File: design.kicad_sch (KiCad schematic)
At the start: 78 parts, among them J1 2601-3108, J10 Conn_01x04, J11 Conn_01x04, J12 Conn_01x03, J13 Conn_01x03, J14 Conn_01x04, J2 2601-3108, J3 2601-3108, J4 TYPE-C-31-M-12, J5 SKEDD-UPDI-4, J6 Conn_01x04, J7 Conn_01x04, J8 Conn_01x04, J9 Conn_01x04, U1 ATtiny1616-S, U2 AP2112K-3.3, U3 CP2105

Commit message: cleanup
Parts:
- added JP4: LED2x2, Jumper:SolderJumper-2_P1.3mm_Open_Pad1.0x1.5mm, symbol Jumper:SolderJumper_2_Open
- JP1: value SolderJumper_2_Bridged -> PC0
- JP2: value SolderJumper_2_Bridged -> PB1
- JP3: value SolderJumper_2_Bridged -> PB2
- TP1, TP2: value TestPoint -> GND
- TP3: value TestPoint -> 3V3
- TP4: value TestPoint -> VDD
- TP5: value TestPoint -> VBUS
- TP6: value RCWCTE -> VDD
- TP7: value RCWCTE -> GND
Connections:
- net LED-out-Bridge: now reaches LED6.1 (DO), LED7.3 (DI)
- net LED-out-Bridge: now also JP4.2 (B)
- net LED-in-Bridge: now reaches LED2.1 (DO), LED3.3 (DI)
- net LED-in-Bridge: now also JP4.1 (A)
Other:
- moved on the sheet: JP1, JP2, JP3

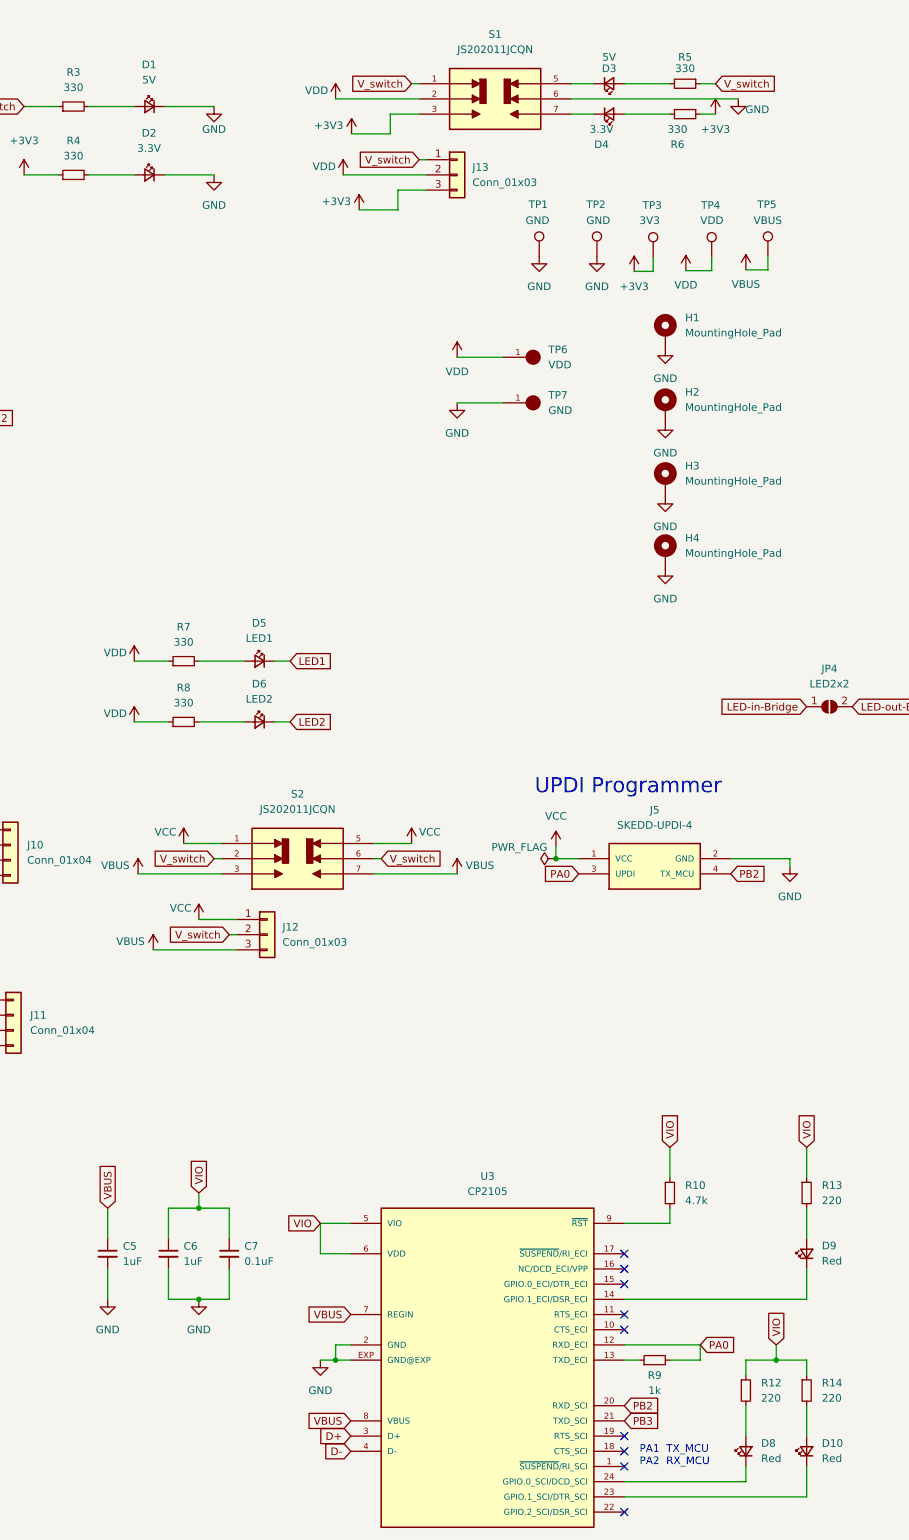
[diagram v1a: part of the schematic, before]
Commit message: add LED color and Parameters
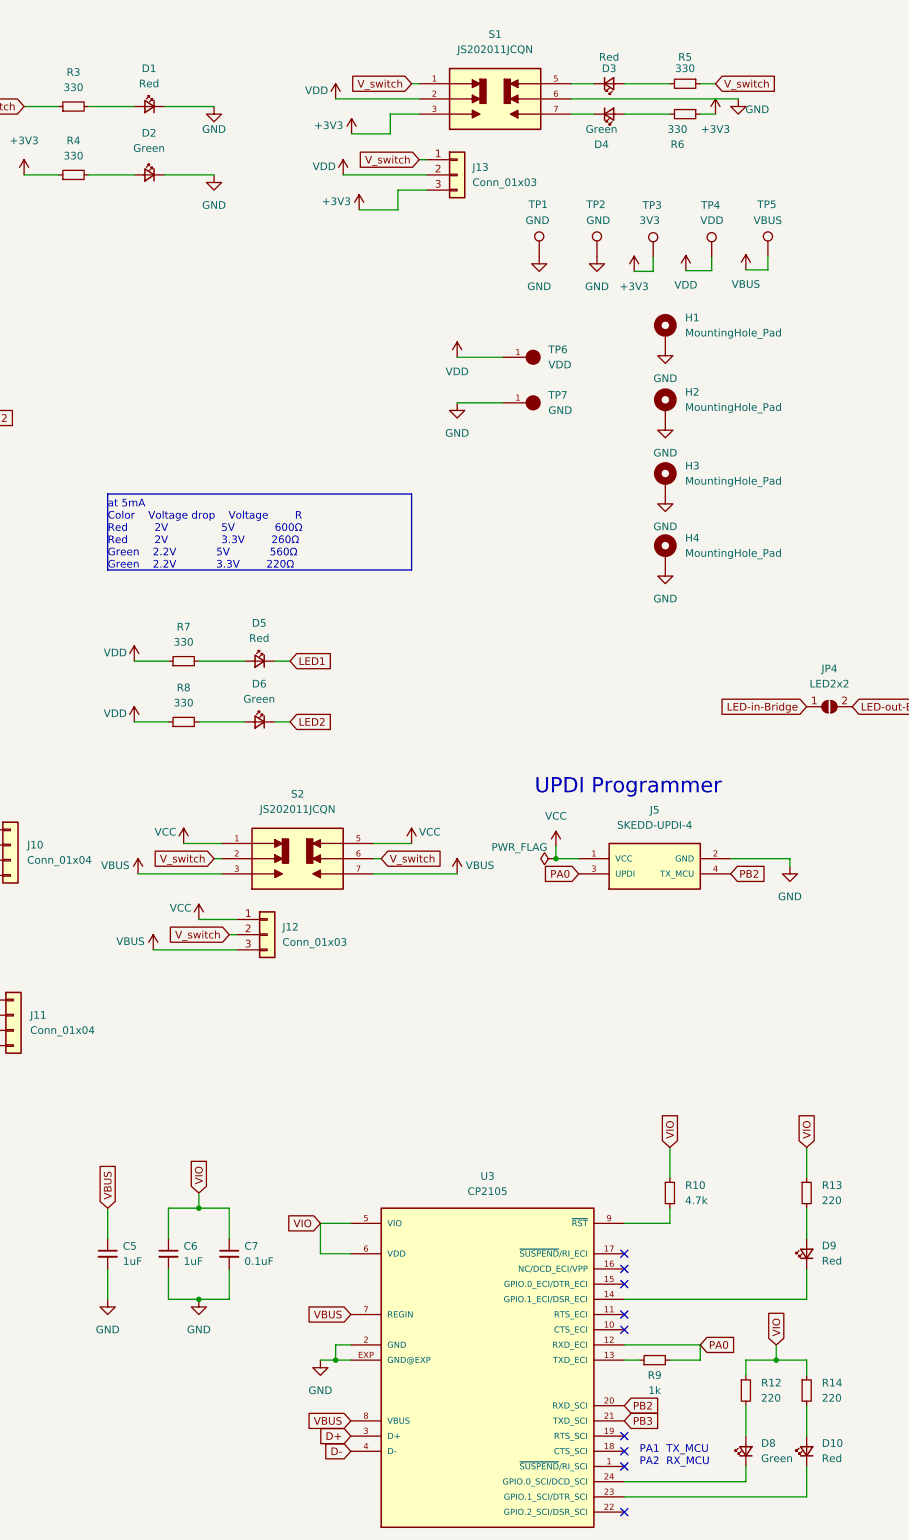
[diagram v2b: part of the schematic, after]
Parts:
- D1, D3: value 5V -> Red
- D2, D4: value 3.3V -> Green
- D5: value LED1 -> Red
- D6: value LED2 -> Green
- D8: value Red -> Green
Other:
- note added: "at 5mA Color Voltage drop Voltage R Red 2V 5V 600Ω Red 2V 3.3V 260Ω Green 2.2V 5V 560Ω Green 2.2V 3.3V 220Ω"
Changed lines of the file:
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@@
     (stroke (width 0) (type default) (color 0 0 0 0))
   )
+  (polyline (pts (xy 213.36 93.98) (xy 213.36 106.68))
+    (stroke (width 0) (type default) (color 0 0 0 0))
+  )
   (wire (pts (xy 182.88 167.64) (xy 184.15 167.64))
     (stroke (width 0) (type default) (color 0 0 0 0))
@@
     (stroke (width 0) (type default) (color 0 0 0 0))
   )
+  (polyline (pts (xy 213.36 106.68) (xy 162.56 106.68))
+    (stroke (width 0) (type default) (color 0 0 0 0))
+  )
   (wire (pts (xy 68.58 27.94) (xy 72.39 27.94))
     (stroke (width 0) (type default) (color 0 0 0 0))
@@
     (stroke (width 0) (type default) (color 0 0 0 0))
   )
+  (polyline (pts (xy 162.56 93.98) (xy 162.56 106.68))
+    (stroke (width 0) (type default) (color 0 0 0 0))
+  )
   (wire (pts (xy 64.77 180.34) (xy 71.12 180.34))
     (stroke (width 0) (type default) (color 0 0 0 0))
@@
     (stroke (width 0) (type default) (color 0 0 0 0))
   )
+  (polyline (pts (xy 162.56 93.98) (xy 213.36 93.98))
+    (stroke (width 0) (type default) (color 0 0 0 0))
+  )
   (wire (pts (xy 358.14 185.42) (xy 358.14 180.34))
     (stroke (width 0) (type default) (color 0 0 0 0))
@@
     (effects (font (size 1.27 1.27)) (justify left bottom))
   )
+  (text "at 5mA\nColor	Voltage drop	Voltage    	R\nRed		2V				5V			600Ω\nRed		2V				3.3V		260Ω\nGreen	2.2V			5V			560Ω\nGreen	2.2V			3.3V		220Ω"
+    (at 162.56 106.68 0)
+    (effects (font (size 1.27 1.27)) (justify left bottom))
+  )
   (text "Output Current: 600mA (Min.)" (at 101.6 58.42 0)
     (effects (font (size 1.27 1.27)) (justify left bottom))
@@
     (in_bom yes) (on_board yes) (fields_autoplaced)
     (property "Reference" "D6" (id 0) (at 187.8965 125.73 0))
-    (property "Value" "LED2" (id 1) (at 187.8965 128.27 0))
+    (property "Value" "Green" (id 1) (at 187.8965 128.27 0))
     (property "Footprint" "LED_SMD:LED_0805_2012Metric" (id 2) (at 187.96 132.08 90)
       (effects (font (size 1.27 1.27)) hide)
@@
     (in_bom yes) (on_board yes) (fields_autoplaced)
     (property "Reference" "D5" (id 0) (at 187.8965 115.57 0))
-    (property "Value" "LED1" (id 1) (at 187.8965 118.11 0))
+    (property "Value" "Red" (id 1) (at 187.8965 118.11 0))
     (property "Footprint" "LED_SMD:LED_0805_2012Metric" (id 2) (at 187.96 121.92 90)
       (effects (font (size 1.27 1.27)) hide)
@@
   (symbol (lib_id "Device:LED_Small") (at 169.545 29.21 0) (mirror y) (unit 1)
     (in_bom yes) (on_board yes) (fields_autoplaced)
-    (property "Reference" "D1" (id 0) (at 169.4815 22.225 0))
-    (property "Value" "5V" (id 1) (at 169.4815 24.765 0))
+    (property "Reference" "D1" (id 0) (at 169.4815 22.86 0))
+    (property "Value" "Red" (id 1) (at 169.4815 25.4 0))
     (property "Footprint" "LED_SMD:LED_0805_2012Metric" (id 2) (at 169.545 29.21 90)
       (effects (font (size 1.27 1.27)) hide)
@@
     (in_bom yes) (on_board yes)
     (property "Reference" "D2" (id 0) (at 169.4815 33.655 0))
-    (property "Value" "3.3V" (id 1) (at 169.4815 36.195 0))
+    (property "Value" "Green" (id 1) (at 169.4815 36.195 0))
     (property "Footprint" "LED_SMD:LED_0805_2012Metric" (id 2) (at 169.545 40.64 90)
       (effects (font (size 1.27 1.27)) hide)
@@
     (in_bom yes) (on_board yes)
     (property "Reference" "D4" (id 0) (at 245.11 35.56 0))
-    (property "Value" "3.3V" (id 1) (at 245.11 33.02 0))
+    (property "Value" "Green" (id 1) (at 245.11 33.02 0))
     (property "Footprint" "LED_SMD:LED_0805_2012Metric" (id 2) (at 246.38 30.48 90)
       (effects (font (size 1.27 1.27)) hide)
@@
     (in_bom yes) (on_board yes)
     (property "Reference" "D3" (id 0) (at 246.38 22.86 0))
-    (property "Value" "5V" (id 1) (at 246.38 20.955 0))
+    (property "Value" "Red" (id 1) (at 246.38 20.955 0))
     (property "Footprint" "LED_SMD:LED_0805_2012Metric" (id 2) (at 246.38 25.4 90)
       (effects (font (size 1.27 1.27)) hide)
@@
       (effects (font (size 1.27 1.27)) (justify right))
     )
-    (property "Value" "Red" (id 1) (at 271.78 255.2064 90)
+    (property "Value" "Green" (id 1) (at 271.78 255.2064 90)
       (effects (font (size 1.27 1.27)) (justify right))
     )
@@
     )
     (path "/5ec38a02-a145-4acb-a554-76dbb10c2abb"
-      (reference "D1") (unit 1) (value "5V") (footprint "LED_SMD:LED_0805_2012Metric")
+      (reference "D1") (unit 1) (value "Red") (footprint "LED_SMD:LED_0805_2012Metric")
     )
     (path "/ab09947a-b17e-4c8a-af0d-4d89f0118870"
-      (reference "D2") (unit 1) (value "3.3V") (footprint "LED_SMD:LED_0805_2012Metric")
+      (reference "D2") (unit 1) (value "Green") (footprint "LED_SMD:LED_0805_2012Metric")
     )
     (path "/c4e31e83-e009-4ac7-b84c-cd948c6ad197"
-      (reference "D3") (unit 1) (value "5V") (footprint "LED_SMD:LED_0805_2012Metric")
+      (reference "D3") (unit 1) (value "Red") (footprint "LED_SMD:LED_0805_2012Metric")
     )
     (path "/c2daad8d-2742-47e3-bd21-622154e104d5"
-      (reference "D4") (unit 1) (value "3.3V") (footprint "LED_SMD:LED_0805_2012Metric")
+      (reference "D4") (unit 1) (value "Green") (footprint "LED_SMD:LED_0805_2012Metric")
     )
     (path "/302ed775-0a92-4094-a83f-5413aa9513d3"
-      (reference "D5") (unit 1) (value "LED1") (footprint "LED_SMD:LED_0805_2012Metric")
+      (reference "D5") (unit 1) (value "Red") (footprint "LED_SMD:LED_0805_2012Metric")
     )
     (path "/29fe1901-f65d-4535-96e4-7f5c316c5cf9"
-      (reference "D6") (unit 1) (value "LED2") (footprint "LED_SMD:LED_0805_2012Metric")
+      (reference "D6") (unit 1) (value "Green") (footprint "LED_SMD:LED_0805_2012Metric")
     )
     (path "/db5ca8c2-4986-41e1-aec1-ef6e7f873716"
-      (reference "D8") (unit 1) (value "Red") (footprint "LED_SMD:LED_0805_2012Metric")
+      (reference "D8") (unit 1) (value "Green") (footprint "LED_SMD:LED_0805_2012Metric")
     )
     (path "/1bc50256-ad94-4b85-ac96-eae729d6ff85"

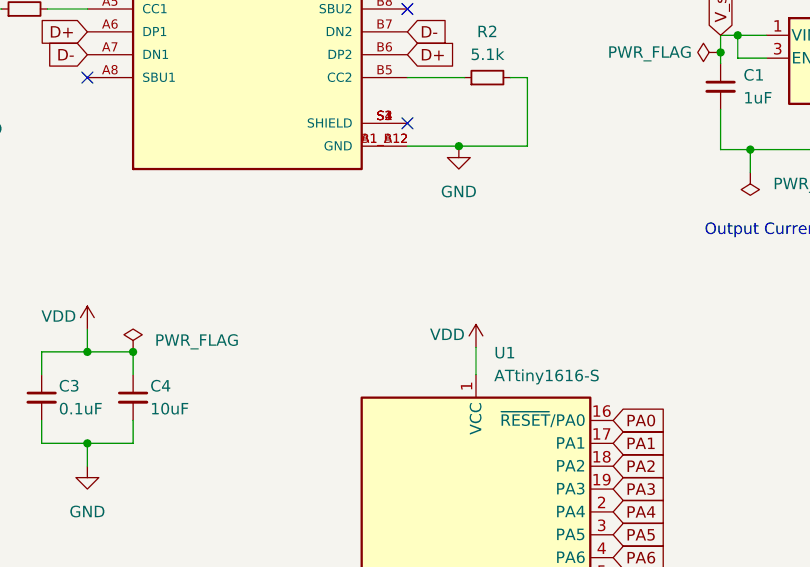
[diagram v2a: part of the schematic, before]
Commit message: Add TVS Diode to USB
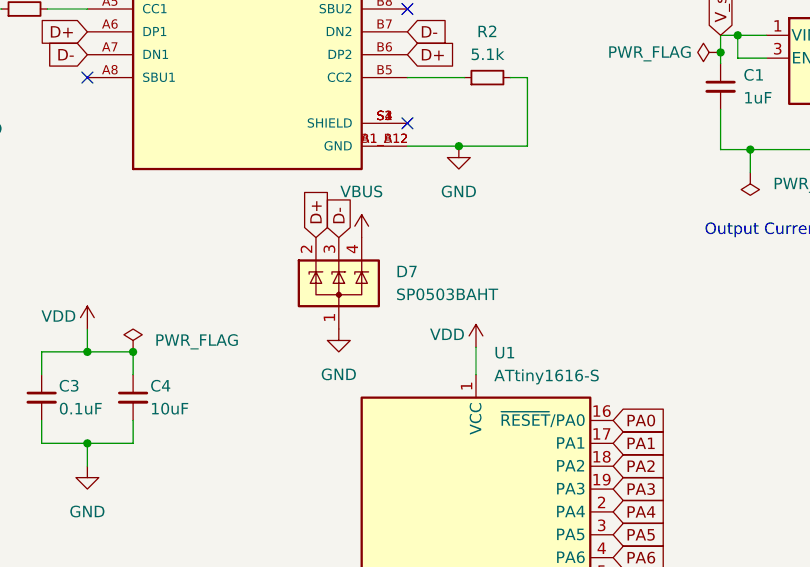
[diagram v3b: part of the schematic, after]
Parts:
- added D7: SP0503BAHT, Package_TO_SOT_SMD:SOT-143, symbol Power_Protection:SP0503BAHT
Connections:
- net D+: now also D7.2 (K)
- net D-: now also D7.3 (K)
- net GND: now also D7.1 (A)
- net VBUS: now also D7.4 (K)
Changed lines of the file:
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@@
     )
   )
+  (global_label "D-" (shape input) (at 60.96 58.42 90) (fields_autoplaced)
+    (effects (font (size 1.27 1.27)) (justify left))
+    (property "Referenzen zwischen Schaltplänen" "${INTERSHEET_REFS}" (id 0) (at 60.8806 53.2534 90)
+      (effects (font (size 1.27 1.27)) (justify left) hide)
+    )
+  )
   (global_label "PA7" (shape input) (at 91.44 96.52 0) (fields_autoplaced)
     (effects (font (size 1.27 1.27)) (justify left))
@@
     )
   )
+  (global_label "D+" (shape input) (at 58.42 58.42 90) (fields_autoplaced)
+    (effects (font (size 1.27 1.27)) (justify left))
+    (property "Referenzen zwischen Schaltplänen" "${INTERSHEET_REFS}" (id 0) (at 58.4994 53.2534 90)
+      (effects (font (size 1.27 1.27)) (justify left) hide)
+    )
+  )
   (global_label "VIO" (shape input) (at 198.12 215.9 180) (fields_autoplaced)
     (effects (font (size 1.27 1.27)) (justify right))
@@
     (pin "4")
   )
+  (symbol (lib_id "power:GND") (at 60.96 68.58 0) (unit 1)
+    (in_bom yes) (on_board yes) (fields_autoplaced)
+    (property "Reference" "#PWR0188" (id 0) (at 60.96 74.93 0)
+      (effects (font (size 1.27 1.27)) hide)
+    )
+    (property "Value" "GND" (id 1) (at 60.96 73.66 0))
+    (property "Footprint" "" (id 2) (at 60.96 68.58 0)
+      (effects (font (size 1.27 1.27)) hide)
+    )
+    (property "Datasheet" "" (id 3) (at 60.96 68.58 0)
+      (effects (font (size 1.27 1.27)) hide)
+    )
+    (pin "1")
+  )
   (symbol (lib_id "power:VCC") (at 175.26 152.4 0) (unit 1)
     (in_bom yes) (on_board yes)
@@
     (pin "1")
   )
+  (symbol (lib_id "Power_Protection:SP0503BAHT") (at 60.96 63.5 0) (unit 1)
+    (in_bom yes) (on_board yes) (fields_autoplaced)
+    (property "Reference" "D7" (id 0) (at 67.31 62.2299 0)
+      (effects (font (size 1.27 1.27)) (justify left))
+    )
+    (property "Value" "SP0503BAHT" (id 1) (at 67.31 64.7699 0)
+      (effects (font (size 1.27 1.27)) (justify left))
+    )
+    (property "Footprint" "Package_TO_SOT_SMD:SOT-143" (id 2) (at 66.675 64.77 0)
+      (effects (font (size 1.27 1.27)) (justify left) hide)
+    )
+    (property "Datasheet" "http://www.littelfuse.com/~/media/files/littelfuse/technical%20resources/documents/data%20sheets/sp05xxba.pdf" (id 3) (at 64.135 60.325 0)
+      (effects (font (size 1.27 1.27)) hide)
+    )
+    (pin "1")
+    (pin "2")
+    (pin "3")
+    (pin "4")
+  )
   (symbol (lib_id "Connector_custom:SKEDD-UPDI-4") (at 254 157.48 0) (unit 1)
     (in_bom yes) (on_board yes) (fields_autoplaced)
@@
     (pin "9")
   )
+  (symbol (lib_id "power:VBUS") (at 63.5 58.42 0) (unit 1)
+    (in_bom yes) (on_board yes)
+    (property "Reference" "#PWR0187" (id 0) (at 63.5 62.23 0)
+      (effects (font (size 1.27 1.27)) hide)
+    )
+    (property "Value" "VBUS" (id 1) (at 63.5 53.34 0))
+    (property "Footprint" "" (id 2) (at 63.5 58.42 0)
+      (effects (font (size 1.27 1.27)) hide)
+    )
+    (property "Datasheet" "" (id 3) (at 63.5 58.42 0)
+      (effects (font (size 1.27 1.27)) hide)
+    )
+    (pin "1")
+  )
   (symbol (lib_id "power:VDD") (at 167.005 121.92 0) (mirror y) (unit 1)
     (in_bom yes) (on_board yes)
@@
       (reference "#PWR0186") (unit 1) (value "GND") (footprint "")
     )
+    (path "/f7c6ca4a-fca9-490e-bc0d-820efe38cb33"
+      (reference "#PWR0187") (unit 1) (value "VBUS") (footprint "")
+    )
+    (path "/78627511-53fb-4339-8132-e29a3fc1aea4"
+      (reference "#PWR0188") (unit 1) (value "GND") (footprint "")
+    )
     (path "/5005112b-a25c-4019-a0f7-bec67dd371e4"
       (reference "C1") (unit 1) (value "1uF") (footprint "Capacitor_SMD:C_0805_2012Metric")
@@
       (reference "D6") (unit 1) (value "Green") (footprint "LED_SMD:LED_0805_2012Metric")
     )
+    (path "/899fa900-a958-4f81-9f44-2529784def90"
+      (reference "D7") (unit 1) (value "SP0503BAHT") (footprint "Package_TO_SOT_SMD:SOT-143")
+    )
     (path "/db5ca8c2-4986-41e1-aec1-ef6e7f873716"
